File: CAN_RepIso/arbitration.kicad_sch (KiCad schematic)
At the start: 14 parts, among them U1 SN74LV32APWR, U2 SN74LVC2G08DCUR, U3 74LVC2G07, U4 74LVC2G07, U5 SN74LVC2G132DCUR

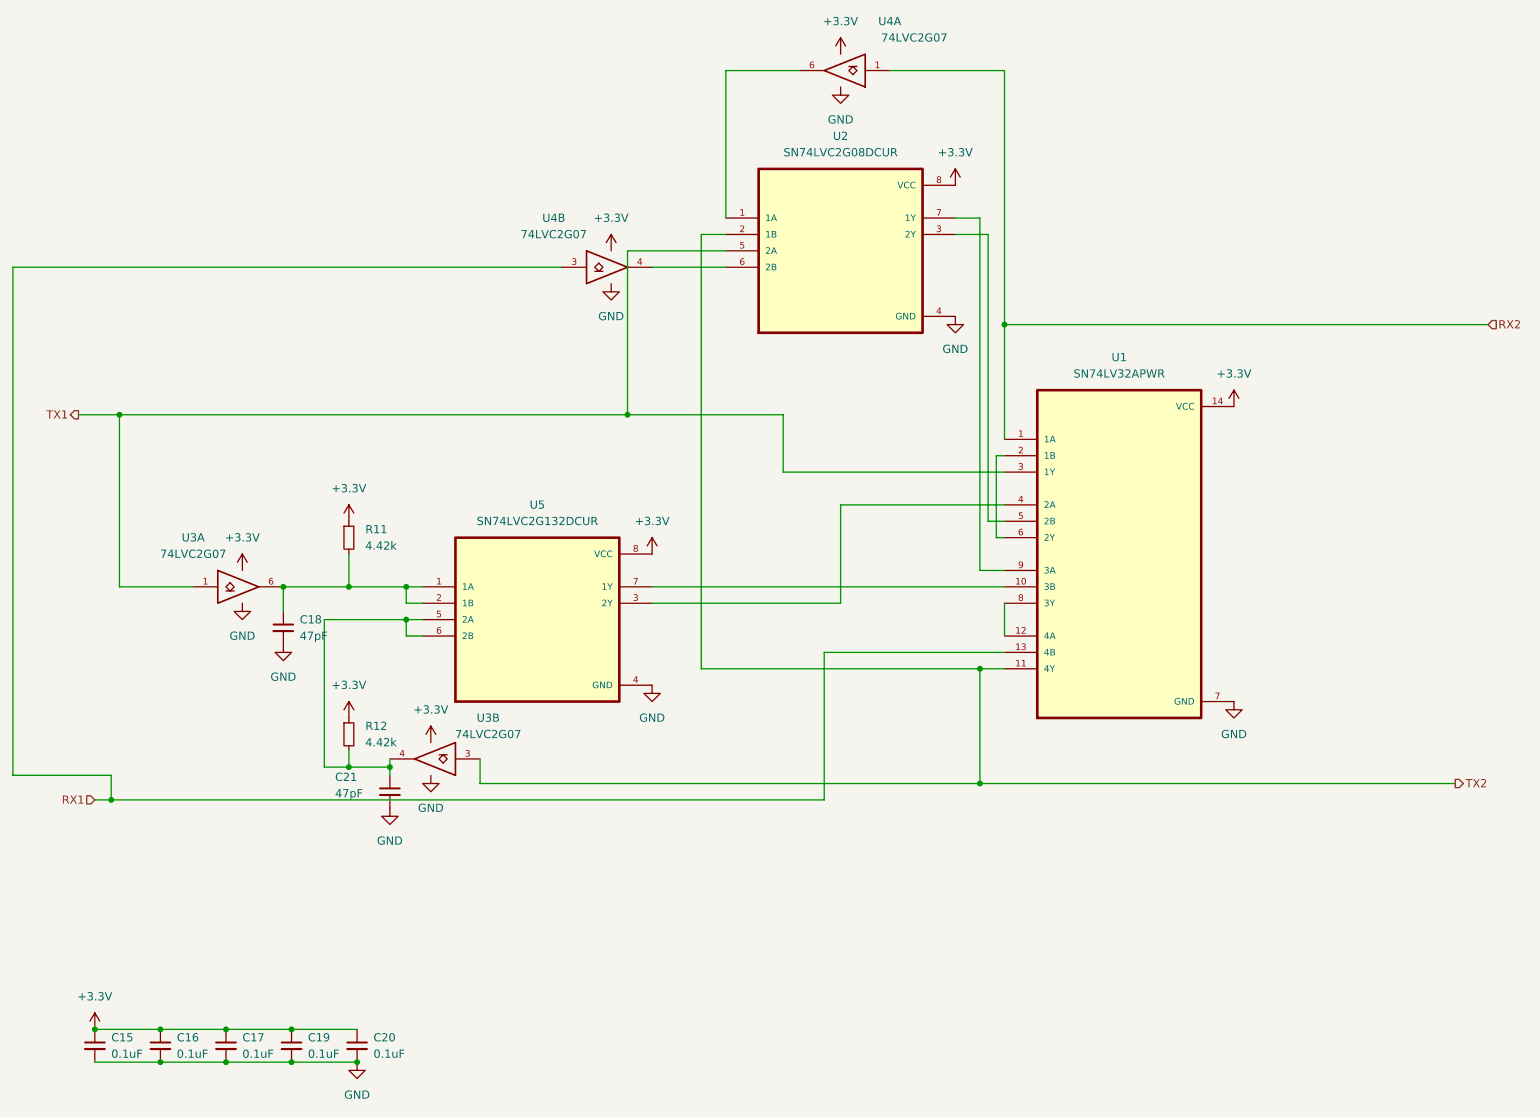
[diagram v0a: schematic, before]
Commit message: Layout done
still needs touchups on the planes and the rounded corner
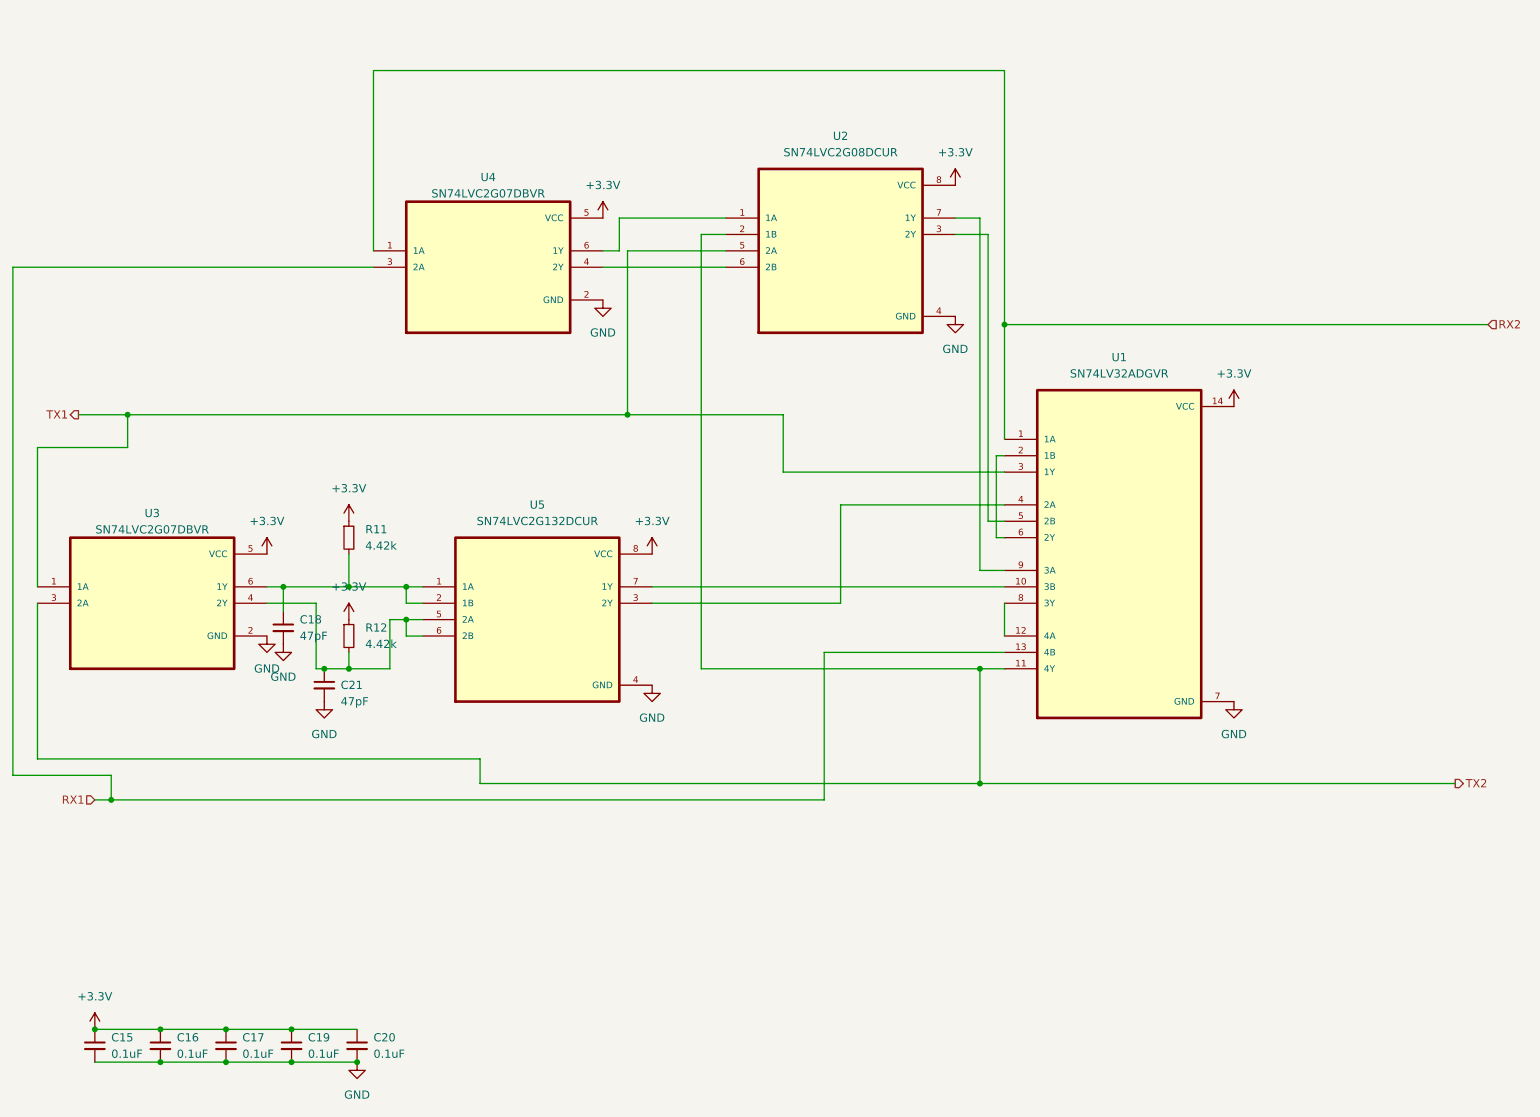
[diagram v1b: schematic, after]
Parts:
- removed U3, U4: 74LVC2G07, symbol 74xGxx:74LVC2G07
- added U3, U4: SN74LVC2G07DBVR, iclr:SOT95P280X145-6N, symbol iclr:SN74LVC2G07DBVR
- U1: value SN74LV32APWR -> SN74LV32ADGVR; footprint SOP65P640X120-14N -> iclr:SOP40P640X120-14N
- U2, U5: footprint SOP50P310X90-8N -> iclr:SOP50P310X90-8N
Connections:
- net +3V3: now also U3.5 (VCC), U4.5 (VCC); no longer C15.2, C16.2, C17.2, C18.2, C19.2, C20.2, C21.2, U1.7 (GND), U2.4 (GND), U5.4 (GND)
- net RX1: now also U4.3 (2A)
- net RX2: now also U4.1 (1A)
- net TX1: now also U3.1 (1A)
- net TX2: now also U3.3 (2A)
- net at C18.1, R11.2, U5.1 (1A)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: now also U3.6 (1Y)
- net at C21.1, R12.2, U5.5 (2A)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: now also U3.4 (2Y)
- net at U2.1 (1A): now also U4.6 (1Y)
- net at U2.6 (2B): now also U4.4 (2Y)
- new net GND: C15.2, C16.2, C17.2, C18.2, C19.2, C20.2, C21.2, U1.7 (GND), U2.4 (GND), U3.2 (GND), U4.2 (GND), U5.4 (GND)
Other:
- moved on the sheet: R12

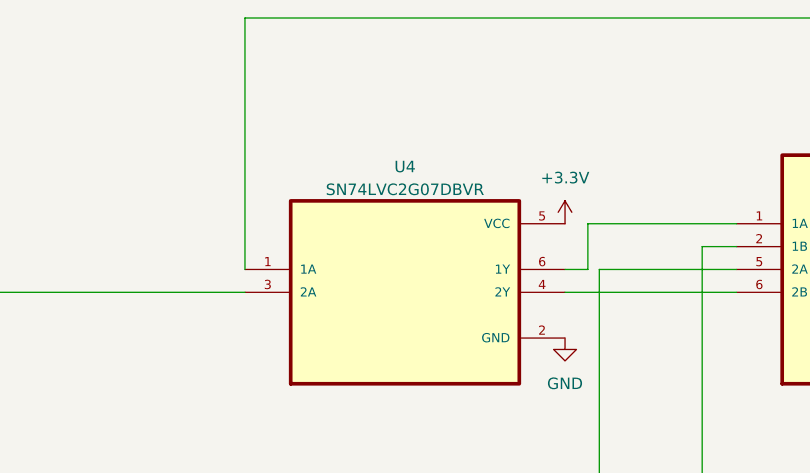
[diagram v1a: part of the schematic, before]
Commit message: changed U4 from driver to NOT gate, implemented review feedback
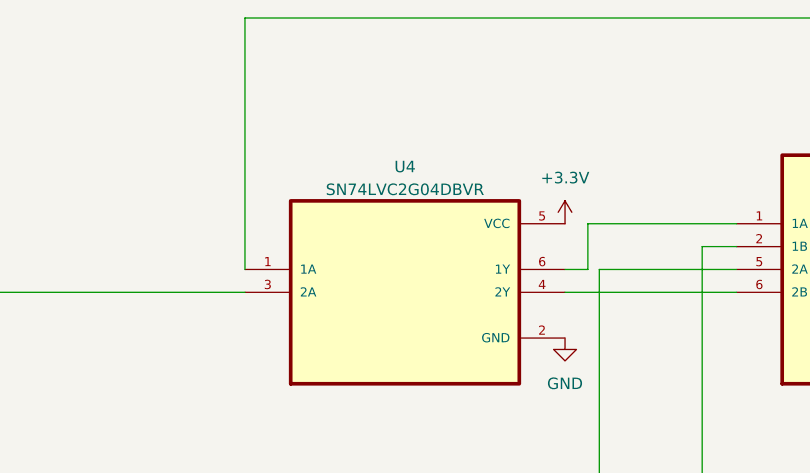
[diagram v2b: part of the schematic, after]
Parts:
- removed U4: SN74LVC2G07DBVR, iclr:SOT95P280X145-6N, symbol iclr:SN74LVC2G07DBVR
- added U4: SN74LVC2G04DBVR, SOT95P280X145-6N, symbol iclr:SN74LVC2G04DBVR
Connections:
- net +3V3: now also U4.5 (VCC)
- net GND: now also U4.2 (GND)
- net RX1: now also U4.3 (2A)
- net RX2: now also U4.1 (1A)
- net at U2.6 (2B): now also U4.4 (2Y)
- net at U2.1 (1A): now also U4.6 (1Y)

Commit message: added option for a 2nd digital isolator
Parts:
- U4: footprint SOT95P280X145-6N -> iclr:SOT95P280X145-6N
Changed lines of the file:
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@@
     (property "Reference" "U4" (id 0) (at 105.41 41.944 0))
     (property "Value" "SN74LVC2G04DBVR" (id 1) (at 105.41 44.4809 0))
-    (property "Footprint" "SOT95P280X145-6N" (id 2) (at 105.41 55.88 0)
+    (property "Footprint" "iclr:SOT95P280X145-6N" (id 2) (at 105.41 55.88 0)
       (effects (font (size 1.27 1.27)) (justify left bottom) hide)
     )

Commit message: v2 finished pre-review
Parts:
- C15, C16, C17, C18, C19, C20, C21: footprint Capacitor_SMD:C_0603_1608Metric -> Capacitor_SMD:C_0402_1005Metric
- R11, R12: footprint Resistor_SMD:R_0603_1608Metric -> Resistor_SMD:R_0402_1005Metric
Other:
- title: (none) -> Arbitration
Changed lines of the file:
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@@
 (kicad_sch (version 20230121) (generator eeschema)
   (paper "A4")
+  (title_block
+    (title "Arbitration")
+    (date "2023-03-30")
+    (rev "1.0")
+  )
   (junction (at 181.61 118.11) (diameter 0) (color 0 0 0 0)
   )
@@
       (effects (font (size 1.27 1.27)) (justify left))
     )
-    (property "Footprint" "Capacitor_SMD:C_0603_1608Metric" (at 85.09 176.53 0)
+    (property "Footprint" "Capacitor_SMD:C_0402_1005Metric" (at 85.09 176.53 0)
       (effects (font (size 1.27 1.27)) hide)
     )
@@
       (effects (font (size 1.27 1.27)) (justify left))
     )
-    (property "Footprint" "Capacitor_SMD:C_0603_1608Metric" (at 64.77 176.53 0)
+    (property "Footprint" "Capacitor_SMD:C_0402_1005Metric" (at 64.77 176.53 0)
       (effects (font (size 1.27 1.27)) hide)
     )
@@
       (effects (font (size 1.27 1.27)) (justify left))
     )
-    (property "Footprint" "Capacitor_SMD:C_0603_1608Metric" (at 44.45 176.53 0)
+    (property "Footprint" "Capacitor_SMD:C_0402_1005Metric" (at 44.45 176.53 0)
       (effects (font (size 1.27 1.27)) hide)
     )
@@
       (effects (font (size 1.27 1.27)) (justify left))
     )
-    (property "Footprint" "Capacitor_SMD:C_0603_1608Metric" (at 54.61 176.53 0)
+    (property "Footprint" "Capacitor_SMD:C_0402_1005Metric" (at 54.61 176.53 0)
       (effects (font (size 1.27 1.27)) hide)
     )
@@
       (effects (font (size 1.27 1.27)) (justify left))
     )
-    (property "Footprint" "Capacitor_SMD:C_0603_1608Metric" (at 74.93 176.53 0)
+    (property "Footprint" "Capacitor_SMD:C_0402_1005Metric" (at 74.93 176.53 0)
       (effects (font (size 1.27 1.27)) hide)
     )
@@
       (effects (font (size 1.27 1.27)) (justify left))
     )
-    (property "Footprint" "Capacitor_SMD:C_0603_1608Metric" (at 73.66 111.76 0)
+    (property "Footprint" "Capacitor_SMD:C_0402_1005Metric" (at 73.66 111.76 0)
       (effects (font (size 1.27 1.27)) hide)
     )
@@
       (effects (font (size 1.27 1.27)) (justify left))
     )
-    (property "Footprint" "Resistor_SMD:R_0603_1608Metric" (at 83.82 113.03 0)
+    (property "Footprint" "Resistor_SMD:R_0402_1005Metric" (at 83.82 113.03 0)
       (effects (font (size 1.27 1.27)) hide)
     )
@@
       (effects (font (size 1.27 1.27)) (justify left))
     )
-    (property "Footprint" "Resistor_SMD:R_0603_1608Metric" (at 83.82 97.79 0)
+    (property "Footprint" "Resistor_SMD:R_0402_1005Metric" (at 83.82 97.79 0)
       (effects (font (size 1.27 1.27)) hide)
     )
@@
       (effects (font (size 1.27 1.27)) (justify left))
     )
-    (property "Footprint" "Capacitor_SMD:C_0603_1608Metric" (at 80.01 120.65 0)
-      (effects (font (size 1.27 1.27)) hide)
-    )
+    (property "Footprint" "Capacitor_SMD:C_0402_1005Metric" (at 80.01 120.65 0)
+      (effects (font (size 1.27 1.27)) hide)
+    )

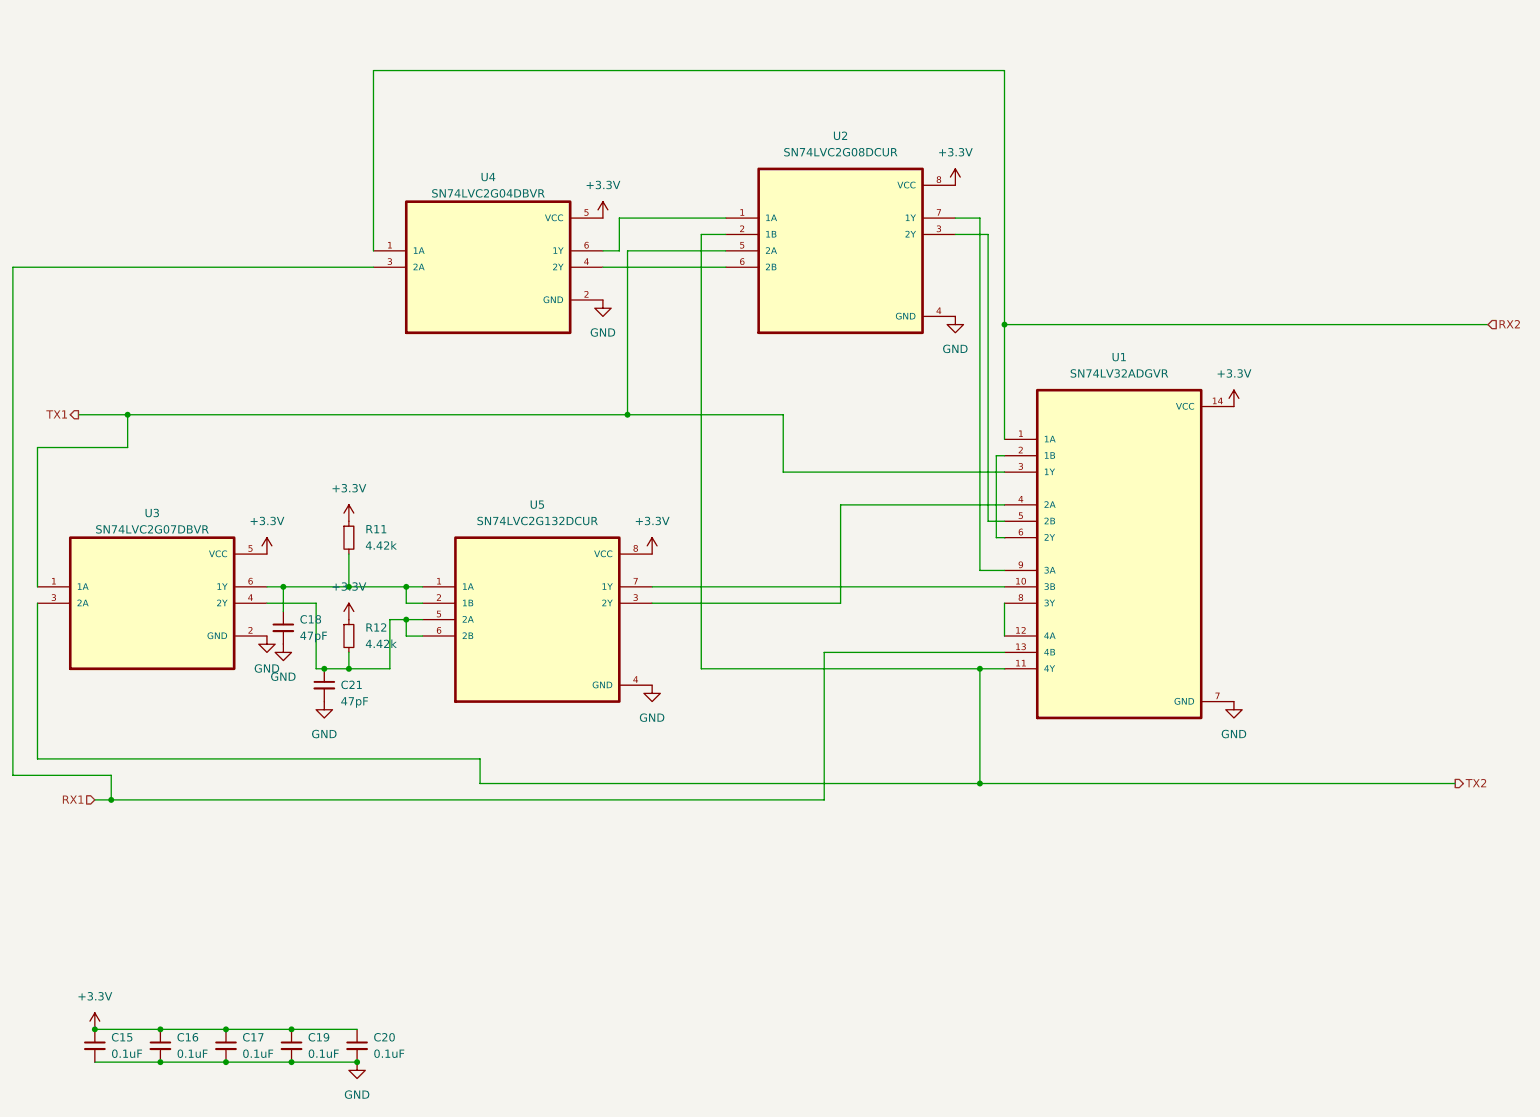
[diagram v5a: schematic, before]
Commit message: clean up schematic and bom
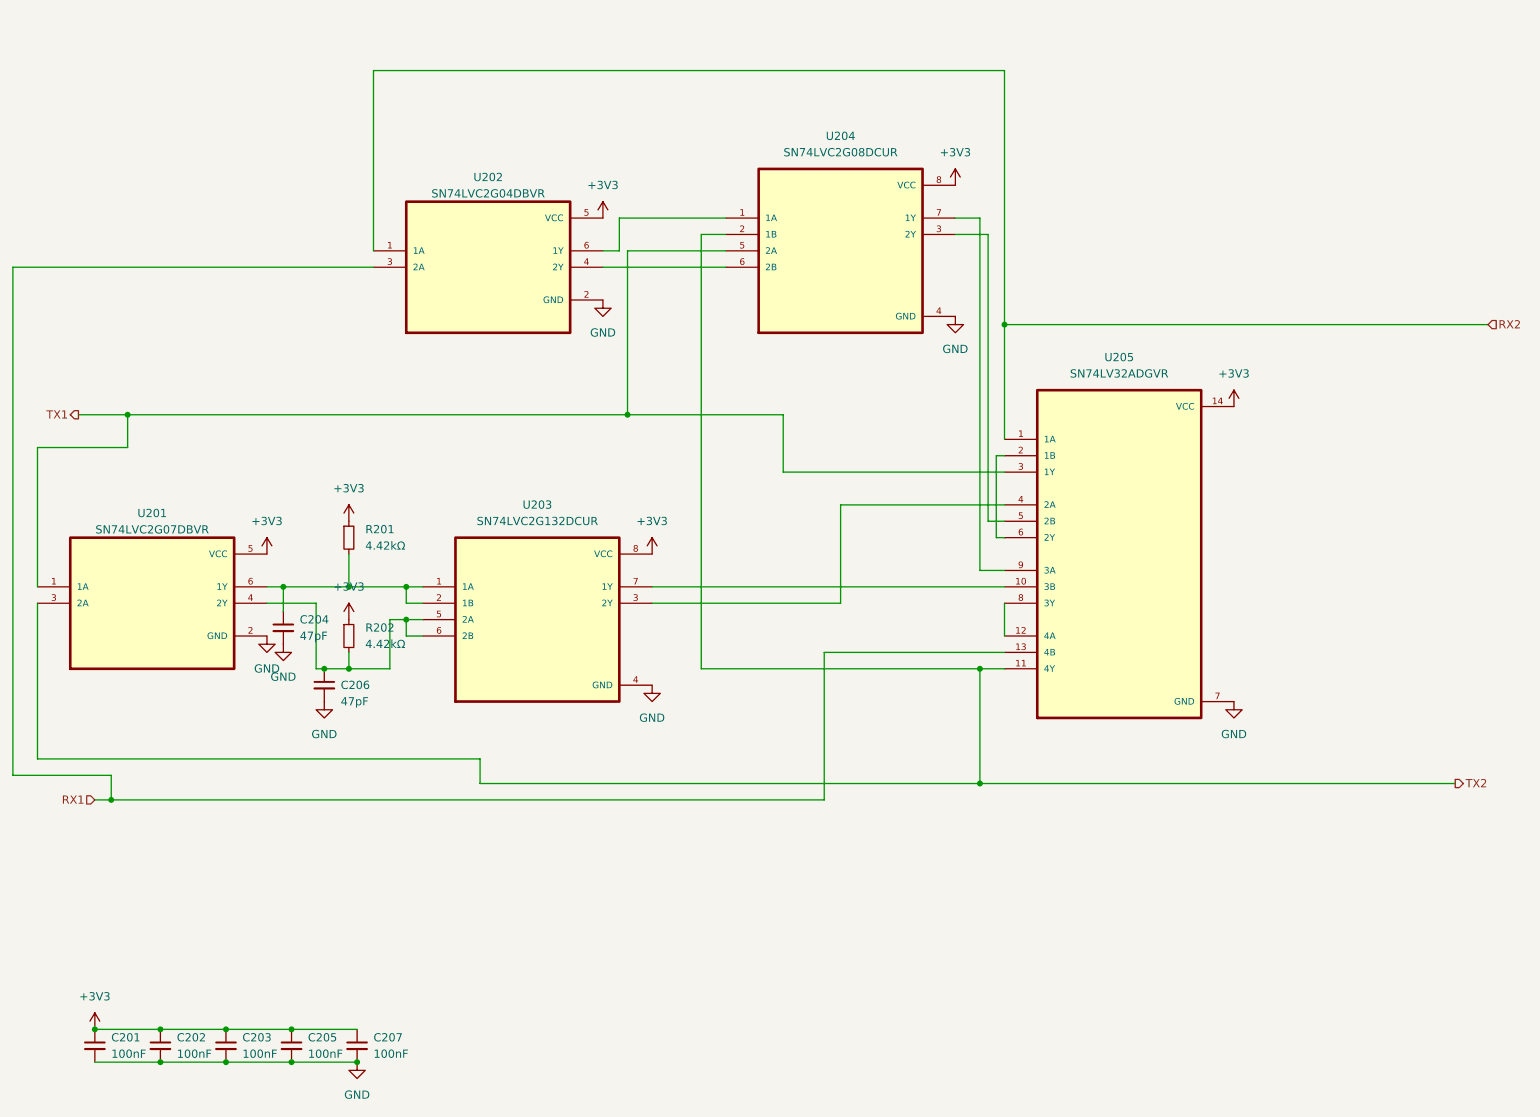
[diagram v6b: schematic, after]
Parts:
- C201: renamed from C15; value 0.1uF -> 100nF
- C202: renamed from C16; value 0.1uF -> 100nF
- C203: renamed from C17; value 0.1uF -> 100nF
- C205: renamed from C19; value 0.1uF -> 100nF
- C207: renamed from C20; value 0.1uF -> 100nF
- R201: renamed from R11; value 4.42k -> 4.42kΩ
- R202: renamed from R12; value 4.42k -> 4.42kΩ
- renumbered C18 to C204, C21 to C206, U3 to U201, U4 to U202, U5 to U203, U2 to U204, U1 to U205
